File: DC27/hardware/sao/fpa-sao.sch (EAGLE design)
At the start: 45 parts, among them IC1 LDL112D33R, U1 ICE40UL1K-SWG16ITR1K, U2 MIC5504-1.2YM5-TR, U3 W25X20CLSNIG

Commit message: checking in sao changes
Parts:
- removed IC1: LDL112D33R, voltage-regulator:LDL112D33R
- removed LED2, LED6, LED7, LED8: (no value), leds:LED3MM
- removed R10, R11, R5, R6, R7, R8, R9: (no value), passives:RESISTOR0805-RES
- removed R4: 10 K, passives:RESISTOR0805-RES
- removed U$12, U$13, U$14, U$15, U$16, U$17, U$18, U$19: APA1025050, leds:APA1025050
- removed U1: ICE40UL1K-SWG16ITR1K, FPGA:ICE40UL1K-SWG16ITR1K
- added C16: 15 pF, passives:C-USC0805
- added C5: 0.1 uF, passives:C-USC0805
- added J1: (no value), connector:M06SILK_FEMALE_PTH
- added J2: FPGA_PROG, connector:M05X2NO_SILK
- added J3, J4: (no value), connector:M18_
- added LED1: (no value), leds:LED3MM
- added R2: 56 R, passives:RESISTOR1206
- added R3: 10 K, passives:RESISTOR0805-RES
- added S1, S2: (no value), switches:SWITCH-SPSTKIT
- added U$1: DC-27-SAO, defcon:DC-27-SAO
- added U$10, U$6, U$7, U$8, U$9: APA1025050, leds:APA1025050
- added U4: MIC5504-3.3YM5-TR, voltage-regulator:MIC5504-3.3YM5-TR
- added U5: ICE5LP1K-SG48ITR, FPGA:ICE5LP1K-SG48ITR
- C10, C11, C12, C13: value 15 pF -> 0.1 uF
- C4: value 1 uF -> 0.1 uF
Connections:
- removed net BARCODE: R10.2, U1.BARCODE_0
- removed net CDONE: R5.2, U1.IOB_8A_G4_CDONE_2
- removed net FLASH_CS: R4.1, U1.IOB_17B_SS_1, U3.!CS
- removed net IRLED: R9.2, U1.IRLED_0
- removed net N$10: U$14.DO, U$17.DI
- removed net N$12: LED4.A, R7.1
- removed net N$13: LED3.A, R6.1
- removed net N$14: LED2.A, R5.1
- removed net N$24: U$12.DO, U$13.DI
- removed net N$25: U$12.CO, U$13.CI
- removed net N$26: U$15.DI, U$16.DO
- removed net N$27: U$15.CI, U$16.CO
- removed net N$28: U$14.DI, U$15.DO
- removed net N$29: U$14.CI, U$15.CO
- removed net N$30: U$13.CO, U$16.CI
- removed net N$31: U$13.DO, U$16.DI
- removed net N$32: U$17.CO, U$18.CI
- removed net N$33: U$17.DO, U$18.DI
- removed net N$34: U$18.DO, U$19.DI
- removed net N$35: U$18.CO, U$19.CI
- removed net N$37: U$14.CO, U$17.CI
- removed net N$9: LED5.A, R8.1
- removed net VCC3.3: R1.2
- removed net VCC5V: C4.2, IC1.EN, IC1.VIN
- new net INIT: J2.8
- new net N$15: U$10.CI, U$8.CO
- new net N$17: U$10.DI, U$8.DO
- new net N$18: U$10.DO, U$11.DI
- new net N$19: U$10.CO, U$11.CI
- new net N$2: R2.2, U5.CDONE
- new net N$21: U$11.CO, U$9.CI
- new net N$22: U$11.DO, U$9.DI
- new net N$3: R1.1, U5.CRESET_B
- new net N$5: U$6.CO, U$7.CI
- new net PROG_FLASH_CS: J1.5, S1.S
- new net SAO_VCC_IN: C1.1, J2.6, U$1.3V3, U4.EN, U4.VIN
- new net SCL: U$1.SCL, U5.IOB_31B
- new net SDA: U$1.SDA, U5.IOB_29B
- new net SPI_CS: R3.2, S1.O, U5.IOB_35B_SPI_CSN
- new net SPI_MEM_CS: S1.P, U3.!CS
- new net TRST: J2.9
- net GND: now also C10.1, C11.1, C12.1, C13.1, C16.2, C5.1, J1.6, J2.2, J2.4, J3.1, J4.18, LED1.C, S2.O, U$1.GND, U$10.GND, U$6.GND, U$7.GND, U$8.GND, U$9.GND, U4.GND, U5.GND; no longer C10.2, C11.2, C12.2, C13.2, IC1.GND(1), IC1.GND(2), IC1.GND(3), IC1.GND(4), LED2.C, LED3.C, LED4.C, LED5.C, LED6.C, LED7.C, LED8.C, U$12.GND, U$13.GND, U$14.GND, U$15.GND, U$16.GND, U$17.GND, U$18.GND, U$19.GND, U1.GND, U1.GND_LED
- net MISO: now also J1.4, J2.5, U5.IOB_32A_SPI_SO; no longer R11.2, U1.IOB_14A_SO_1
- net MOSI: now also J1.3, J2.7, U$6.DI, U5.IOB_33B_SPI_SI; no longer U$11.DI, U1.IOB_15B_SI_1
- net N$1: now also LED1.A, R2.1; no longer U$11.CO, U$12.CI
- net N$23: now also J2.3; no longer U$11.DO, U$12.DI
- net N$4: now also R3.1, S2.P; no longer R1.1, U1.CRESET_B_2
- net N$6: now also U$6.DO, U$7.DI; no longer LED8.A, R11.1
- net N$7: now also U$7.DO, U$8.DI; no longer LED7.A, R10.1
- net N$8: now also U$7.CO, U$8.CI; no longer LED6.A, R9.1
- net RGB0: now also LED3.C, U5.RGB0; no longer R6.2, U1.RGB0_0
- net RGB1: now also LED4.C, U5.RGB1; no longer R7.2, U1.RGB1_0
- net RGB2: now also LED5.C, U5.RGB2; no longer R8.2, U1.RGB2_0
- net SCK: now also J1.2, J2.1, U$6.CI, U5.IOB_34A_SPI_SCK; no longer U$11.CI, U1.IOB_16A_SCK_1
- net VCC1.2V: now also C12.2, C13.2, J4.1, U5.VCC, U5.VCCPLL; no longer U1.VCC
- net VCC3.3V: now also C10.2, C11.2, C16.1, C4.2, C5.2, J1.1, J3.18, LED3.A, LED4.A, LED5.A, R1.2, S2.S, U$10.VCC, U$6.VCC, U$7.VCC, U$8.VCC, U4.VOUT, U5.SPI_VCCIO1, U5.VCCIO_0, U5.VCCIO_2, U5.VPP_2V5; no longer C1.1, C10.1, C11.1, C12.1, C13.1, IC1.VOUT, R4.2, U$12.VCC, U$13.VCC, U$14.VCC, U$15.VCC, U$16.VCC, U$17.VCC, U$18.VCC, U$19.VCC, U1.SPI_VCCIO1_VCCIO2, U1.VPP_2V5_VCCIO0
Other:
- note added: "RGB LED Pins are Open Drain outpus and sink current not source current."
- note removed: "The iCE40-1KLP SWG16 package CDONE pin can be used as a user output."

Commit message: updated sao
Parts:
- removed U$11, U$9: APA1025050, leds:APA1025050
- added C17, C18: 15 pF, passives:C-USC0805
- added U$2, U$3, U$4, U$5: APA1025050, leds:APA1025050
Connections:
- removed net N$18: U$10.DO, U$11.DI
- removed net N$19: U$10.CO, U$11.CI
- removed net N$21: U$11.CO, U$9.CI
- removed net N$22: U$11.DO, U$9.DI
- new net MOSI-2: U$2.DI, U5.IOT_37A
- new net N$12: U$2.DO, U$3.DI
- new net N$13: U$3.DO, U$4.DI
- new net N$14: U$3.CO, U$4.CI
- new net N$15: U$4.DO, U$5.DI
- new net N$17: U$4.CO, U$5.CI
- new net N$9: U$2.CO, U$3.CI
- new net SCK-2: U$2.CI, U5.IOT_39A
- net GND: now also C17.2, C18.2, U$2.GND, U$3.GND, U$4.GND, U$5.GND; no longer U$11.GND, U$9.GND
- net VCC3.3V: now also C17.1, C18.1, U$2.VCC, U$3.VCC, U$4.VCC, U$5.VCC; no longer U$11.VCC
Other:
- moved on the sheet: C12, C14, C16, C7

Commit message: updated sao and docs
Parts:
- added J5: (no value), connector:M06SILK_FEMALE_PTH
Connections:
- removed net N$3: R1.1, U5.CRESET_B
- new net 0A: J3.13, U5.IOB_0A
- new net 16A: J3.8, U5.IOB_16A
- new net 18A: J3.7, U5.IOB_18A
- new net 20A: J3.6, U5.IOB_20A
- new net 22A: J3.5, U5.IOB_22A
- new net 23B: J4.17, U5.IOB_23B
- new net 24A: J3.4, U5.IOB_24A
- new net 25B: J3.15, U5.IOB_25B_G3
- new net 2A: J3.12, U5.IOB_2A
- new net 36B: J4.8, U5.IOT_36B
- new net 38B: J4.9, U5.IOT_38B
- new net 3B: J3.14, U5.IOB_3B_G6
- new net 41A: J4.4, U5.IOT_41A
- new net 42B: J4.10, U5.IOT_42B
- new net 43A: J4.5, U5.IOT_43A
- new net 44B: J4.11, U5.IOT_44B
- new net 45A: J3.16, U5.IOT_45A_G1
- new net 46B: J3.17, U5.IOT_46B_G0
- new net 48B: J4.12, U5.IOT_48B
- new net 49A: J4.6, U5.IOT_49A
- new net 4A: J3.11, U5.IOB_4A
- new net 50B: J4.13, U5.IOT_50B
- new net 51A: J4.7, U5.IOT_51A
- new net 5B: J3.3, U5.IOB_5B
- new net 6A: J3.10, U5.IOB_6A
- new net 8A: J3.9, U5.IOB_8A
- new net 9B: J3.2, U5.IOB_9B
- new net CRESET: R1.1, U5.CRESET_B, U5.IOB_13B
- net GND: now also J5.1
- net MOSI-2: now also J4.2
- net RGB0: now also J4.14
- net RGB1: now also J4.15
- net RGB2: now also J4.16
- net SAO_VCC_IN: now also J5.2
- net SCK-2: now also J4.3
- net SCL: now also J5.4
- net SDA: now also J5.5
- net VCC1.2V: now also J5.3
- net VCC3.3V: now also J5.6
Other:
- moved on the sheet: J3, J4, LED3, LED4, LED5

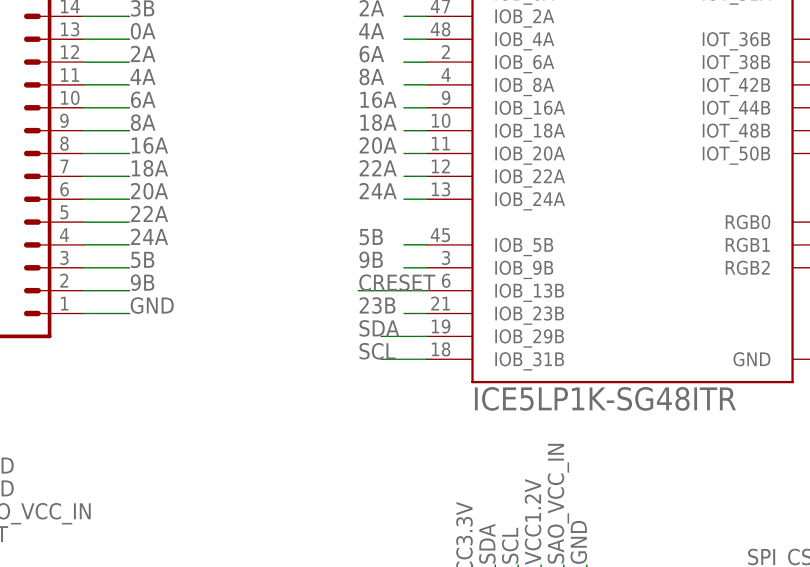
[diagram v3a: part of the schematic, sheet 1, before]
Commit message: tied pin 6 to cdone
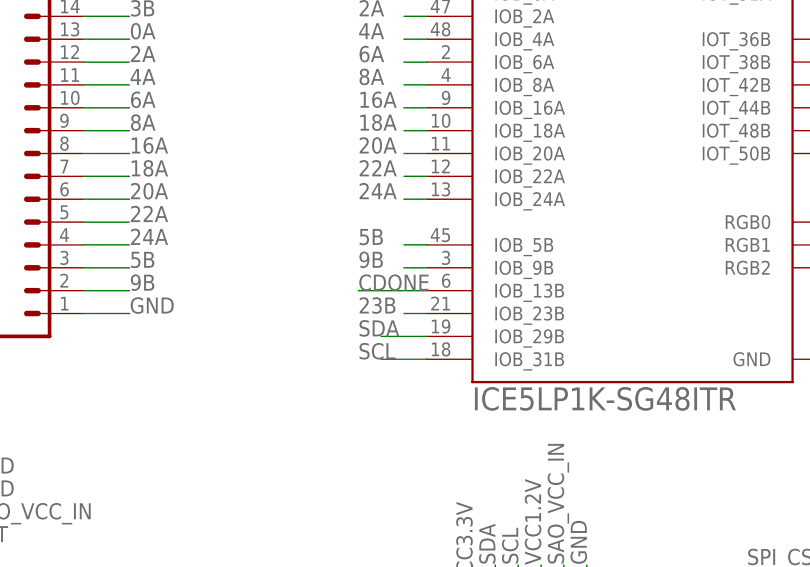
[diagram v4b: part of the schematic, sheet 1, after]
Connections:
- new net CDONE: U5.IOB_13B
- net CRESET: no longer U5.IOB_13B
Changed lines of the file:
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@@
 <label x="-7.62" y="104.14" size="1.778" layer="95"/>
-</segment>
-<segment>
-<pinref part="U5" gate="G$1" pin="IOB_13B"/>
-<wire x1="25.4" y1="43.18" x2="17.78" y2="43.18" width="0.1524" layer="91"/>
-<label x="17.78" y="43.18" size="1.778" layer="95"/>
 </segment>
 </net>
@@
 </segment>
 </net>
+<net name="CDONE" class="0">
+<segment>
+<pinref part="U5" gate="G$1" pin="IOB_13B"/>
+<wire x1="25.4" y1="43.18" x2="17.78" y2="43.18" width="0.1524" layer="91"/>
+<label x="17.78" y="43.18" size="1.778" layer="95"/>
+</segment>
+</net>

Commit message: final tweaks moved top board I2C to separate bus
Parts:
- removed J1, J5: (no value), connector:M06SILK_FEMALE_PTH
- removed J3, J4: (no value), connector:M18_
- added C19: 0.1 uF, passives:C-USC0603
- added J6, J7: (no value), connector:M20NO_SILK_KIT
- added U$9: CMD_C0DE_LOGOCMD_CODE_LOGO_SILK, logos:CMD_C0DE_LOGOCMD_CODE_LOGO_SILK
- C1, C10, C11, C12, C13, C15, C2, C3, C4, C5: device passives:C-USC0805 -> passives:C-USC0603
- C14, C16, C17, C18, C6, C7, C8, C9: device passives:C-USC0805 -> passives:C-USC1206
- LED1: device leds:LED3MM -> leds:LED1206
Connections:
- removed net 25B: J3.15, U5.IOB_25B_G3
- removed net 36B: J4.8, U5.IOT_36B
- removed net 6A: J3.10, U5.IOB_6A
- removed net 8A: J3.9, U5.IOB_8A
- removed net N$2: R2.2, U5.CDONE
- removed net N$23: J2.3
- removed net TRST: J2.9
- new net 37A: J6.4, U5.IOT_37A
- net 0A: now also J7.16; no longer J3.13
- net 16A: now also J7.10; no longer J3.8
- net 18A: now also J7.9; no longer J3.7
- net 20A: now also J7.8; no longer J3.6
- net 22A: now also J7.7; no longer J3.5
- net 23B: now also J6.5; no longer J4.17
- net 24A: now also J7.6; no longer J3.4
- net 2A: now also J7.15; no longer J3.12
- net 38B: now also J6.10; no longer J4.9
- net 3B: now also J7.18; no longer J3.14
- net 41A: now also J6.11; no longer J4.4
- net 42B: now also J6.14; no longer J4.10
- net 43A: now also J6.15; no longer J4.5
- net 44B: now also J6.16; no longer J4.11
- net 45A: now also J6.19; no longer J3.16
- net 46B: now also J6.17; no longer J3.17
- net 48B: now also J6.18; no longer J4.12
- net 49A: now also J7.19; no longer J4.6
- net 4A: now also J7.14; no longer J3.11
- net 50B: now also J6.20; no longer J4.13
- net 51A: now also J7.20; no longer J4.7
- net 5B: now also J7.17; no longer J3.3
- net 9B: now also J7.12; no longer J3.2
- net CDONE: now also R2.2, U5.CDONE
- net CRESET: now also J2.9
- net GND: now also C19.1, J6.13, J6.2, J6.3, J7.1; no longer J1.6, J3.1, J4.18, J5.1
- net MISO: now also J7.3; no longer J1.4
- net MOSI: now also J7.4; no longer J1.3
- net MOSI-2: now also J6.9, U5.IOT_39A; no longer J4.2, U5.IOT_37A
- net PROG_FLASH_CS: now also J7.2; no longer J1.5
- net RGB0: no longer J4.14
- net RGB1: no longer J4.15
- net RGB2: no longer J4.16
- net SAO_VCC_IN: no longer J5.2
- net SCK: now also J7.5; no longer J1.2
- net SCK-2: now also J6.8, U5.IOT_36B; no longer J4.3, U5.IOT_39A
- net SCL: now also J6.6; no longer J5.4
- net SDA: now also J6.7; no longer J5.5
- net VCC1.2V: now also C19.2, C5.2, J7.11; no longer C12.2, J4.1, J5.3
- net VCC3.3V: now also C12.2, J6.12, J7.13; no longer C5.2, J1.1, J3.18, J5.6
